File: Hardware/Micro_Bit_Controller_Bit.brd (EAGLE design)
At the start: 152.4 x 50.8 mm, 52 parts, among them J1 Pokehome, J2 Pokehome, J3 Pokehome, J4 Pokehome, J5 Pokehome, J6 Pokehome, J7 Pokehome, J8 Pokehome, J9 QWIIC_RA, U2 micro:bit

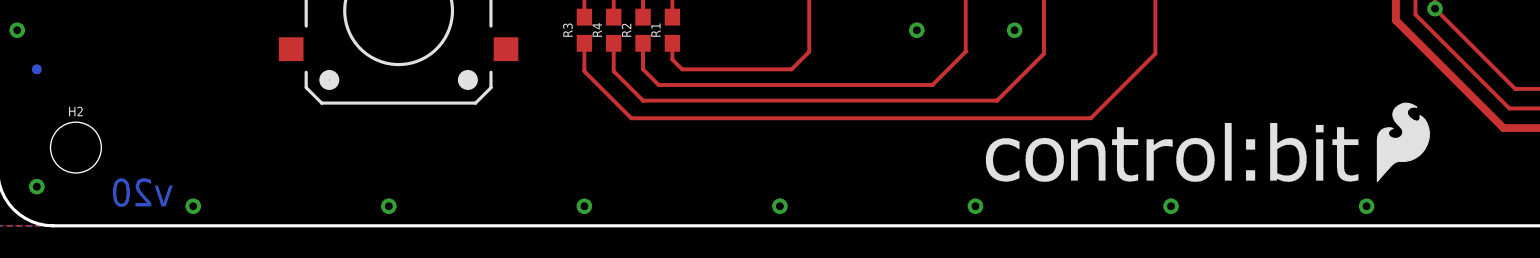
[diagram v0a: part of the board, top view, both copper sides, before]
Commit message: Control:bit logo to Controller:bit
Also bumped version to v21 in brd and sch, to ensure correct panel files are used.
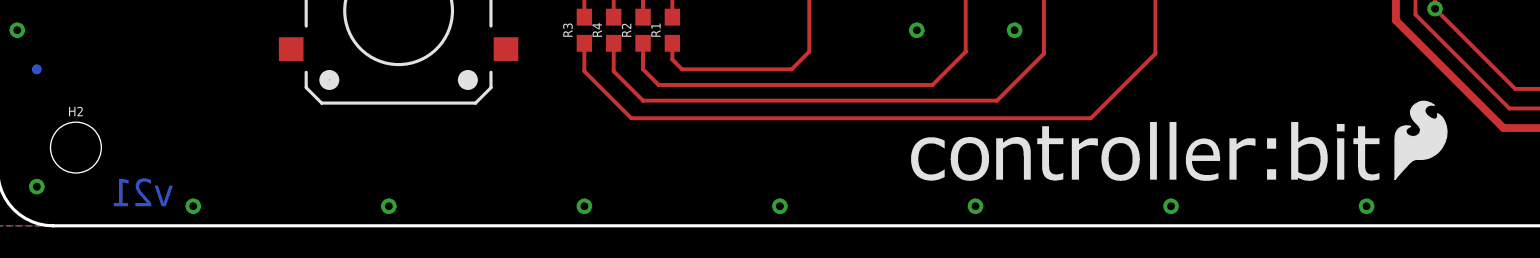
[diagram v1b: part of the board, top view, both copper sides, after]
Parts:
- removed U$4, U$5: LOGO-CONTROLBIT, SparkFun-Aesthetics:LOGO-CONTROLBIT
- added U$3, U$6: LOGO-CONTROLLER_BIT, SparkFun-Aesthetics:LOGO-CONTROLLER_BIT
- moved LOGO1 1.15 mm to (90.4, 2.73)
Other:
- board text added: "v21"
- board text removed: "v20"
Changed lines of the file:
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@@
 <?xml version="1.0" encoding="utf-8"?>
 <!DOCTYPE eagle SYSTEM "eagle.dtd">
-<eagle version="9.5.1">
+<eagle version="9.5.2">
 <drawing>
 <settings>
@@
 <text x="137.16" y="48.895" size="1.27" layer="22" font="vector" ratio="15" rot="MR0" align="bottom-center">P12</text>
 <text x="146.05" y="48.895" size="1.27" layer="22" font="vector" ratio="15" rot="MR0" align="bottom-center">P16</text>
-<text x="11.43" y="1.27" size="1.778" layer="16" font="vector" ratio="15" rot="MR0">v20</text>
+<text x="11.43" y="1.27" size="1.778" layer="16" font="vector" ratio="15" rot="MR0">v21</text>
 <dimension x1="0" y1="50.8" x2="152.4" y2="50.8" x3="76.2" y3="88.265" textsize="1.778" textratio="15" layer="47" unit="inch"/>
 <dimension x1="152.4" y1="0" x2="152.4" y2="50.8" x3="168.91" y3="25.4" textsize="1.778" textratio="15" layer="47" unit="inch"/>
@@
 <attribute name="PROD_ID" value="CONN-13512" x="146.05" y="41.275" size="1.778" layer="28" font="vector" ratio="15" rot="MR270" display="off"/>
 </element>
-<element name="LOGO1" library="SparkFun-Aesthetics" package="SFE_LOGO_FLAME_.2" value="SFE_LOGO_FLAME.2_INCH" x="89.24925" y="2.6035" smashed="yes"/>
+<element name="LOGO1" library="SparkFun-Aesthetics" package="SFE_LOGO_FLAME_.2" value="SFE_LOGO_FLAME.2_INCH" x="90.39225" y="2.7305" smashed="yes"/>
 <element name="LOGO2" library="SparkFun-Aesthetics" package="OSHW-LOGO-L" value="OSHW-LOGOL" x="76.2" y="24.13" smashed="yes" rot="MR0"/>
 <element name="LOGO3" library="SparkFun-Aesthetics" package="SFE_LOGO_NAME_FLAME_.3" value="SFE_LOGO_NAME_FLAME.3_INCH" x="92.71" y="34.29" smashed="yes" rot="MR0"/>
@@
 <attribute name="VALUE" x="95.25" y="15.24" size="1.27" layer="27" font="vector"/>
 </element>
-<element name="U$4" library="SparkFun-Aesthetics" package="LOGO-CONTROLBIT" value="LOGO-CONTROLBIT" x="64.03975" y="2.8575" smashed="yes"/>
-<element name="U$5" library="SparkFun-Aesthetics" package="LOGO-CONTROLBIT" value="LOGO-CONTROLBIT" x="87.78875" y="30.2895" smashed="yes" rot="MR0"/>
 <element name="J9" library="SparkFun-Connectors" package="JST04_1MM_RA" value="QWIIC_RA" x="126.492" y="45.593" smashed="yes" rot="MR180">
 <attribute name="NAME" x="126.508" y="41.02666875" size="0.6096" layer="26" rot="MR180"/>
@@
 <element name="TP12" library="SparkFun-Connectors" package="PAD.03X.05" value="TEST-POINT3X5" x="63.5" y="29.21" smashed="yes" rot="MR90"/>
 <element name="TP13" library="SparkFun-Connectors" package="PAD.03X.05" value="TEST-POINT3X5" x="60.96" y="29.21" smashed="yes" rot="MR90"/>
+<element name="U$3" library="SparkFun-Aesthetics" package="LOGO-CONTROLLER_BIT" value="LOGO-CONTROLLER_BIT" x="59.182" y="2.921" smashed="yes"/>
+<element name="U$6" library="SparkFun-Aesthetics" package="LOGO-CONTROLLER_BIT" value="LOGO-CONTROLLER_BIT" x="91.059" y="30.734" smashed="yes" rot="MR0"/>
 </elements>
 <signals>

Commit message: Schematic cleanup
-removed pesky test point values (overlap)
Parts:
- TP1, TP10, TP11, TP12, TP13, TP2, TP3, TP4, TP5, TP6, TP7, TP8, TP9: value TEST-POINT3X5 -> (none)
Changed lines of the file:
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@@
 </element>
 <element name="U$2" library="SparkFun-Aesthetics" package="QWIIC_5MM" value="" x="126.7714" y="43.6372" smashed="yes" rot="MR0"/>
-<element name="TP1" library="SparkFun-Connectors" package="PAD.03X.05" value="TEST-POINT3X5" x="81.28" y="29.21" smashed="yes" rot="MR90"/>
-<element name="TP2" library="SparkFun-Connectors" package="PAD.03X.05" value="TEST-POINT3X5" x="88.9" y="29.21" smashed="yes" rot="MR90"/>
-<element name="TP3" library="SparkFun-Connectors" package="PAD.03X.05" value="TEST-POINT3X5" x="58.42" y="29.21" smashed="yes" rot="MR90"/>
-<element name="TP4" library="SparkFun-Connectors" package="PAD.03X.05" value="TEST-POINT3X5" x="86.36" y="29.21" smashed="yes" rot="MR90"/>
-<element name="TP5" library="SparkFun-Connectors" package="PAD.03X.05" value="TEST-POINT3X5" x="83.82" y="29.21" smashed="yes" rot="MR90"/>
-<element name="TP6" library="SparkFun-Connectors" package="PAD.03X.05" value="TEST-POINT3X5" x="78.74" y="29.21" smashed="yes" rot="MR90"/>
-<element name="TP7" library="SparkFun-Connectors" package="PAD.03X.05" value="TEST-POINT3X5" x="76.2" y="29.21" smashed="yes" rot="MR90"/>
-<element name="TP8" library="SparkFun-Connectors" package="PAD.03X.05" value="TEST-POINT3X5" x="73.66" y="29.21" smashed="yes" rot="MR90"/>
-<element name="TP9" library="SparkFun-Connectors" package="PAD.03X.05" value="TEST-POINT3X5" x="71.12" y="29.21" smashed="yes" rot="MR90"/>
-<element name="TP10" library="SparkFun-Connectors" package="PAD.03X.05" value="TEST-POINT3X5" x="68.58" y="29.21" smashed="yes" rot="MR90"/>
-<element name="TP11" library="SparkFun-Connectors" package="PAD.03X.05" value="TEST-POINT3X5" x="66.04" y="29.21" smashed="yes" rot="MR90"/>
-<element name="TP12" library="SparkFun-Connectors" package="PAD.03X.05" value="TEST-POINT3X5" x="63.5" y="29.21" smashed="yes" rot="MR90"/>
-<element name="TP13" library="SparkFun-Connectors" package="PAD.03X.05" value="TEST-POINT3X5" x="60.96" y="29.21" smashed="yes" rot="MR90"/>
+<element name="TP1" library="SparkFun-Connectors" package="PAD.03X.05" value="" x="81.28" y="29.21" smashed="yes" rot="MR90"/>
+<element name="TP2" library="SparkFun-Connectors" package="PAD.03X.05" value="" x="88.9" y="29.21" smashed="yes" rot="MR90"/>
+<element name="TP3" library="SparkFun-Connectors" package="PAD.03X.05" value="" x="58.42" y="29.21" smashed="yes" rot="MR90"/>
+<element name="TP4" library="SparkFun-Connectors" package="PAD.03X.05" value="" x="86.36" y="29.21" smashed="yes" rot="MR90"/>
+<element name="TP5" library="SparkFun-Connectors" package="PAD.03X.05" value="" x="83.82" y="29.21" smashed="yes" rot="MR90"/>
+<element name="TP6" library="SparkFun-Connectors" package="PAD.03X.05" value="" x="78.74" y="29.21" smashed="yes" rot="MR90"/>
+<element name="TP7" library="SparkFun-Connectors" package="PAD.03X.05" value="" x="76.2" y="29.21" smashed="yes" rot="MR90"/>
+<element name="TP8" library="SparkFun-Connectors" package="PAD.03X.05" value="" x="73.66" y="29.21" smashed="yes" rot="MR90"/>
+<element name="TP9" library="SparkFun-Connectors" package="PAD.03X.05" value="" x="71.12" y="29.21" smashed="yes" rot="MR90"/>
+<element name="TP10" library="SparkFun-Connectors" package="PAD.03X.05" value="" x="68.58" y="29.21" smashed="yes" rot="MR90"/>
+<element name="TP11" library="SparkFun-Connectors" package="PAD.03X.05" value="" x="66.04" y="29.21" smashed="yes" rot="MR90"/>
+<element name="TP12" library="SparkFun-Connectors" package="PAD.03X.05" value="" x="63.5" y="29.21" smashed="yes" rot="MR90"/>
+<element name="TP13" library="SparkFun-Connectors" package="PAD.03X.05" value="" x="60.96" y="29.21" smashed="yes" rot="MR90"/>
 <element name="U$3" library="SparkFun-Aesthetics" package="LOGO-CONTROLLER_BIT" value="LOGO-CONTROLLER_BIT" x="59.182" y="2.921" smashed="yes"/>
 <element name="U$6" library="SparkFun-Aesthetics" package="LOGO-CONTROLLER_BIT" value="LOGO-CONTROLLER_BIT" x="91.059" y="30.734" smashed="yes" rot="MR0"/>
